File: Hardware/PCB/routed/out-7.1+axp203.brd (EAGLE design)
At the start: 99.1 x 65.7 mm, 191 parts, among them IC2 LM3671MF-1.8, IC3 AXP203H, IC4 TPS562200DBV, J3 USB-A-FEMALE, Q1 24Mhz, Q2 32kHz, U1 SN65LVDS84AQDGGRQ1, U2 W25Q32FV, X2 87758-1216

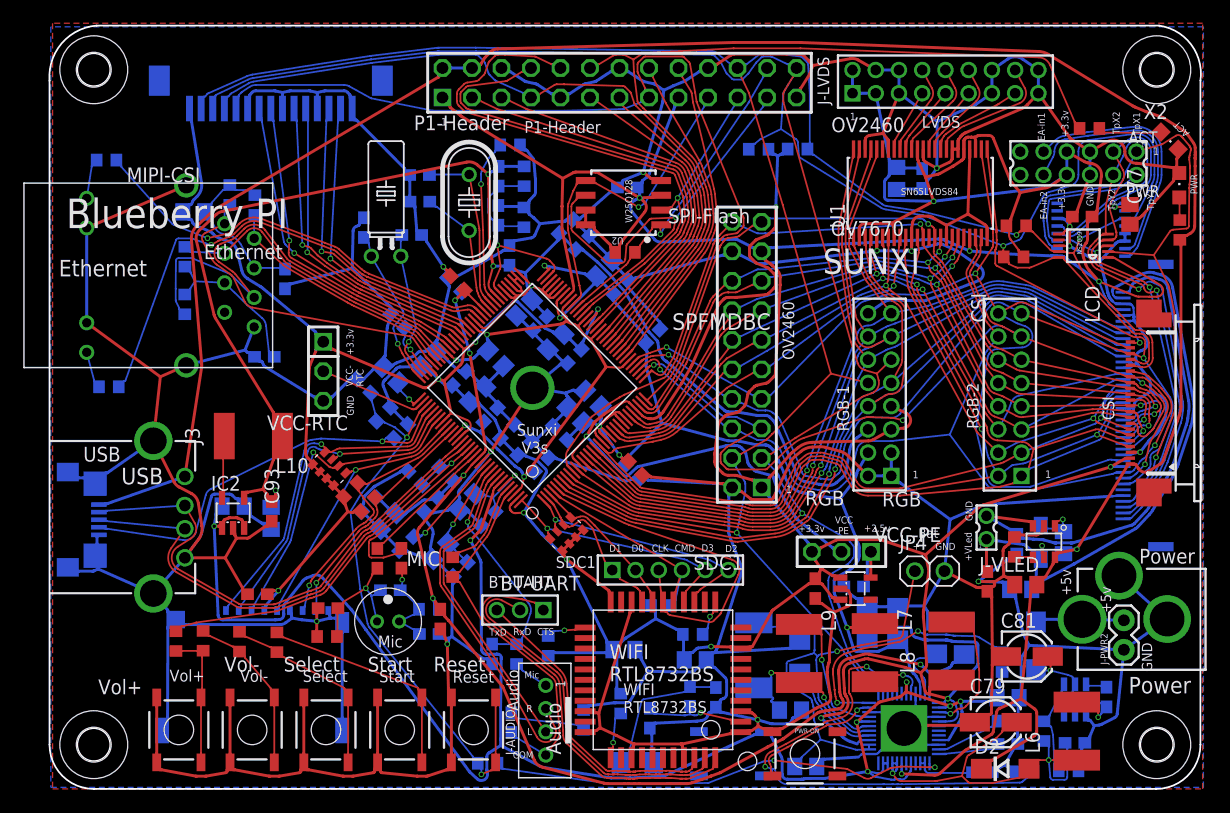
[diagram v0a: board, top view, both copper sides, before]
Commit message: tracing of BBPi*AXP203 was upbated
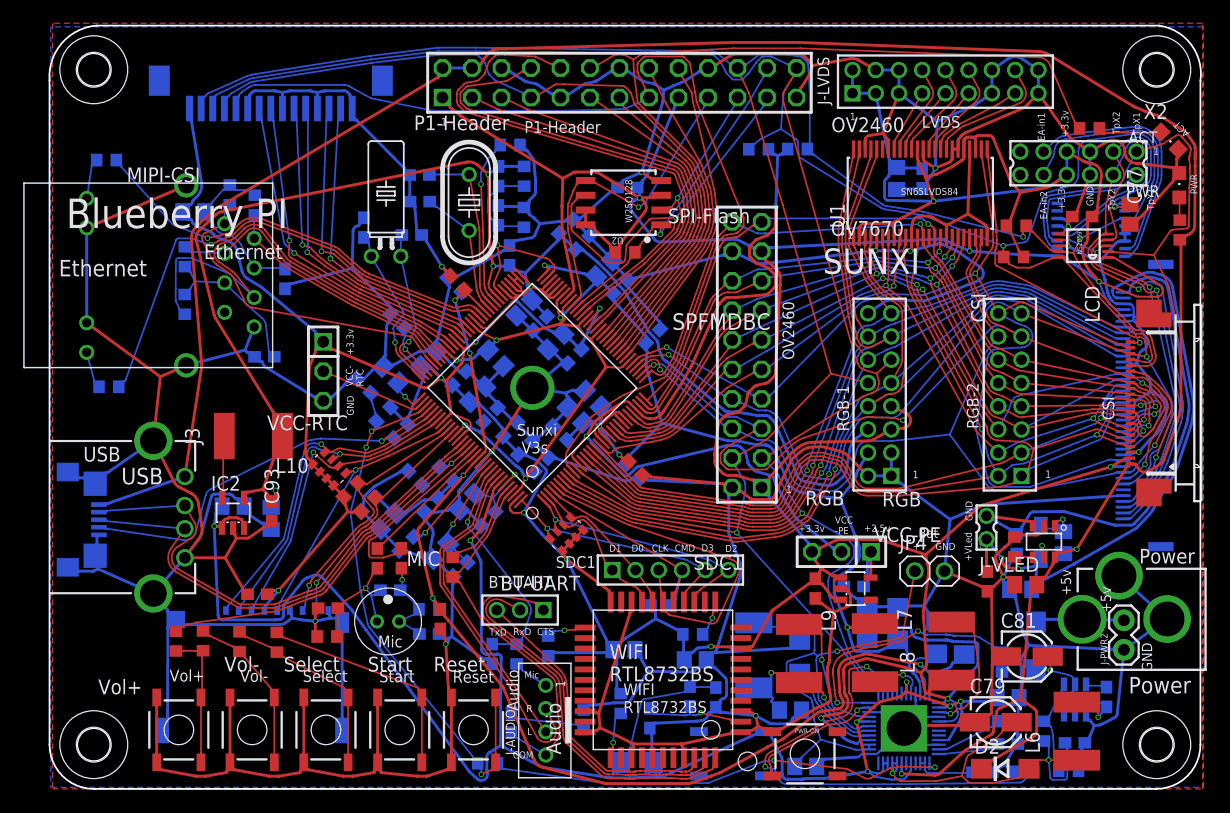
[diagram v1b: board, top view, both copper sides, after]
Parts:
- moved C60 0.31 mm to (39.7, 30.9)
- moved C57 0.07 mm to (40.9, 29.4)
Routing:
- net GND: track 967.2 -> 963.0 mm
- net VLED+: track 53.2 -> 54.2 mm, vias 1 -> 3
- net !RESET: track 50.3 -> 49.3 mm, vias 2 -> 3
- net USB/ID: track 35.1 -> 34.3 mm
- net VLED-: track 44.4 -> 45.1 mm
- net I2C1/SDA: track 191.1 -> 191.7 mm
- net +3V3: track 530.9 -> 530.3 mm
- net I2C1/SCL: track 222.9 -> 223.5 mm
- net N$29: track 12.7 -> 13.3 mm
- net SDC0/D2: track 29.2 -> 28.7 mm
